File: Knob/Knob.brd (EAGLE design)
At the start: 36.3 x 29.8 mm, 18 parts, among them SW1 TopUp EC12PLRGBSDVBF-D, U1 ATTINY48/88-TQFP

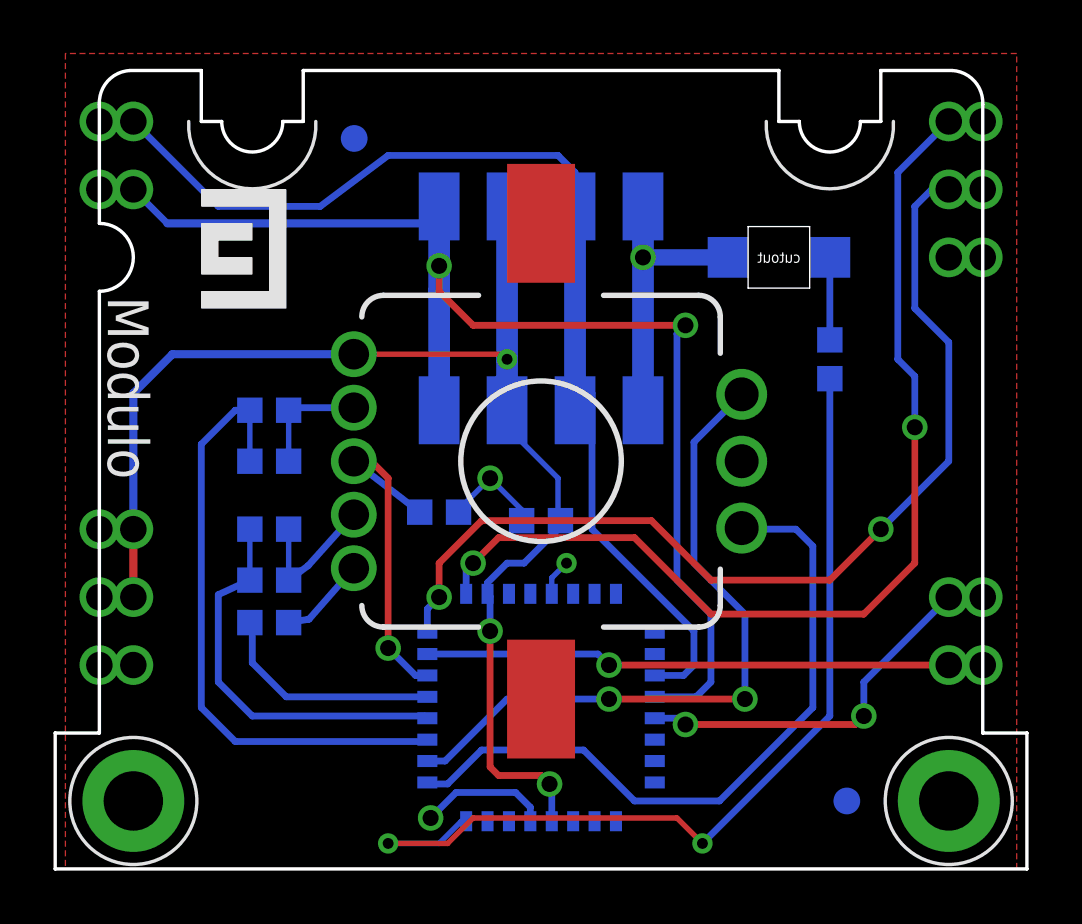
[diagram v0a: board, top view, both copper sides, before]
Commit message: Check point of current PCB designs. Among other things I think this change includes rewiring of programming lines on many of the boards,.
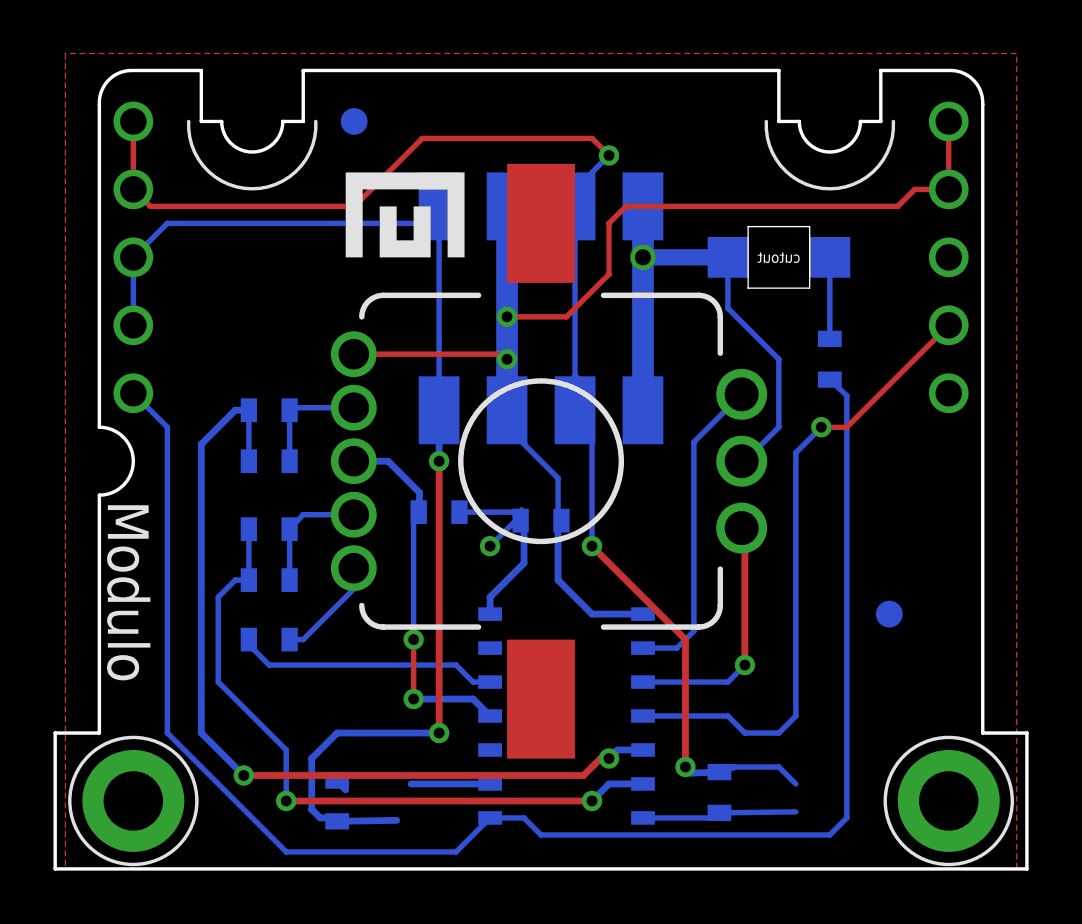
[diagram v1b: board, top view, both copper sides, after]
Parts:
- removed U$1: (no value), Modulo:LOGO-SMALL
- removed U1: ATTINY48/88-TQFP, Modulo:TQFP-32
- added R8, R9: 150Ω, Modulo:0603
- added U2: ATTINY841, Modulo:SOIC-14
- moved F1 7.16 mm to (30.8, 9.53)
- moved U$3 6.67 mm to (12.4, 23.5), turned to 0 degrees
- moved U$2 2.84 mm to (6.99, 21.0), flipped to the bottom, turned to 0 degrees
- moved F2 0.64 mm to (10.8, 27.9)
- moved R2 0.63 mm to (7.62, 8.57)
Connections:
- removed net LED: R7.2, U1.8
- removed net MISO: PCB1.MISO, U1.16
- removed net MOSI: PCB1.MOSI, U1.15
- removed net SCK: PCB1.CLK, U1.17
- new net MISO/LED: PCB1.MISO, R7.2, U2.8
- new net SCL/SCK: R8.2, U2.9
- new net SDA/MOSI: R9.2, U2.7
- net A: now also U2.3; no longer U1.9
- net B: now also U2.2; no longer U1.10
- net BLUE: now also U2.5; no longer U1.11
- net GND: now also U2.14; no longer U1.21, U1.5
- net GREEN: now also U2.6; no longer U1.12
- net RED: now also U2.12; no longer U1.13
- net RESET: now also U2.4; no longer U1.29
- net SCL: now also PCB1.CLK, R8.1; no longer U1.28
- net SDA: now also PCB1.MOSI, R9.1; no longer U1.27
- net SW: now also U2.11; no longer U1.14
- net VCC: now also U2.1; no longer U1.18, U1.4
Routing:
- net MISO/LED: track 0.00 -> 58.2 mm
- net SCK: track 37.7 -> 0.00 mm, vias 2 -> 0
- net MISO: track 36.8 -> 0.00 mm, vias 2 -> 0
- net LED: track 35.1 -> 0.00 mm, vias 2 -> 0
- net MOSI: track 19.7 -> 0.00 mm, vias 1 -> 0
- net A: track 26.2 -> 9.30 mm, vias 0 -> 1
- net B: track 25.7 -> 11.8 mm, vias 2 -> 0
- net SDA: track 43.1 -> 54.7 mm, vias 0 -> 3
- net GREEN: track 14.8 -> 25.6 mm, vias 0 -> 2
- net RESET: track 13.8 -> 23.8 mm, vias 2 -> 1
- net BLUE: track 23.5 -> 32.7 mm, vias 0 -> 2
- net GND: track 20.9 -> 28.5 mm, vias 4 -> 2
- net SDA/MOSI: track 0.00 -> 5.78 mm
- net SCL/SCK: track 0.00 -> 3.42 mm
- net SCL: track 47.8 -> 44.6 mm
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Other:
- outline, holes or cut-outs redrawn

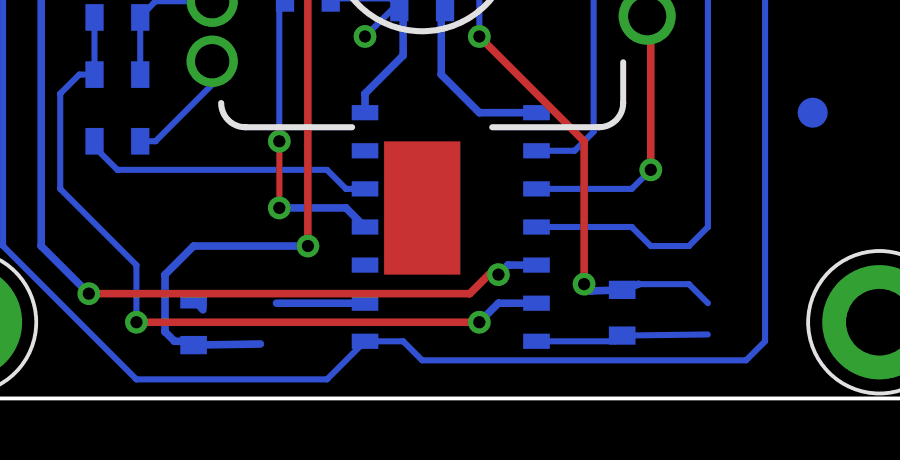
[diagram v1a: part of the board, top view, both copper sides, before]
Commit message: Fixed missing trace on SCL/SCK net.
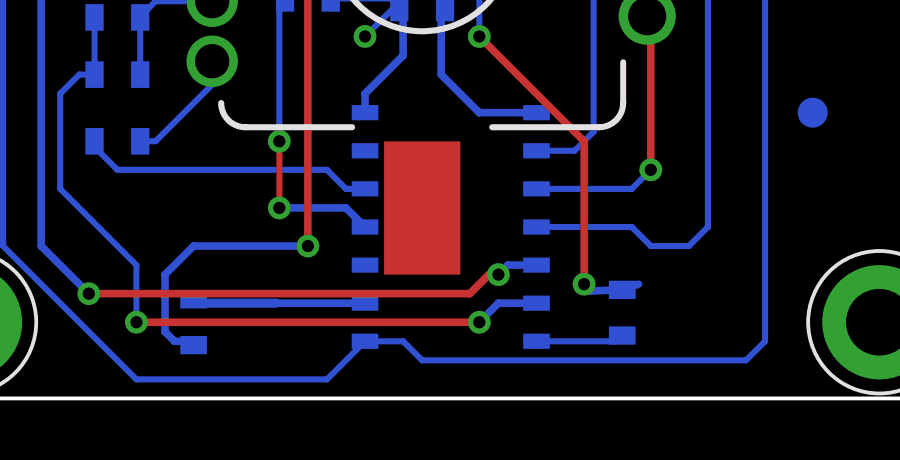
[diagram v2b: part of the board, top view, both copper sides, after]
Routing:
- net SDA/MOSI: track 5.78 -> 2.93 mm
- net SDA: track 54.7 -> 52.1 mm
- net SCL/SCK: track 3.42 -> 5.84 mm
- net SCL: track 44.6 -> 42.4 mm
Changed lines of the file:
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@@
 <layer number="17" name="Pads" color="2" fill="1" visible="yes" active="yes"/>
 <layer number="18" name="Vias" color="2" fill="1" visible="yes" active="yes"/>
-<layer number="19" name="Unrouted" color="6" fill="1" visible="no" active="yes"/>
+<layer number="19" name="Unrouted" color="6" fill="1" visible="yes" active="yes"/>
 <layer number="20" name="Dimension" color="15" fill="1" visible="yes" active="yes"/>
 <layer number="21" name="tPlace" color="7" fill="1" visible="yes" active="yes"/>
@@
 <contactref element="JP1" pad="P$7"/>
 <contactref element="R8" pad="1"/>
-<wire x1="10.16" y1="1.778" x2="12.3869" y2="1.815" width="0.254" layer="16"/>
 <via x="13.97" y="5.08" extent="1-16" drill="0.4064"/>
 <wire x1="13.97" y1="5.08" x2="13.97" y2="15.24" width="0.254" layer="1"/>
@@
 <wire x1="19.05" y1="18.415" x2="19.05" y2="17.145" width="0.2032" layer="16"/>
 <contactref element="R9" pad="1"/>
-<wire x1="27.305" y1="3.175" x2="26.67" y2="3.81" width="0.2032" layer="16"/>
-<wire x1="26.67" y1="3.81" x2="24.9925" y2="3.81" width="0.2032" layer="16"/>
 <wire x1="24.9925" y1="3.81" x2="24.4475" y2="3.6195" width="0.254" layer="16"/>
 <wire x1="24.4475" y1="3.6195" x2="23.405" y2="3.5825" width="0.254" layer="16"/>
@@
 <contactref element="R9" pad="2"/>
 <contactref element="U2" pad="7"/>
-<wire x1="24.4475" y1="2.0955" x2="27.3006" y2="2.1325" width="0.2032" layer="16"/>
 <wire x1="21.59" y1="1.905" x2="24.22" y2="1.905" width="0.2032" layer="16"/>
 <wire x1="24.22" y1="1.905" x2="24.4475" y2="2.0955" width="0.2032" layer="16"/>
@@
 <contactref element="U2" pad="9"/>
 <wire x1="15.875" y1="3.175" x2="12.9231" y2="3.175" width="0.254" layer="16"/>
-<wire x1="10.4731" y1="2.9519" x2="10.16" y2="3.302" width="0.254" layer="16"/>
-<wire x1="10.4731" y1="2.9519" x2="12.9231" y2="3.175" width="0" layer="19" extent="16-16"/>
+<wire x1="12.9231" y1="3.175" x2="10.16" y2="3.175" width="0.3048" layer="16"/>
+<wire x1="10.16" y1="3.175" x2="10.16" y2="3.302" width="0.3048" layer="16"/>
 </signal>
 <signal name="MISO/LED">

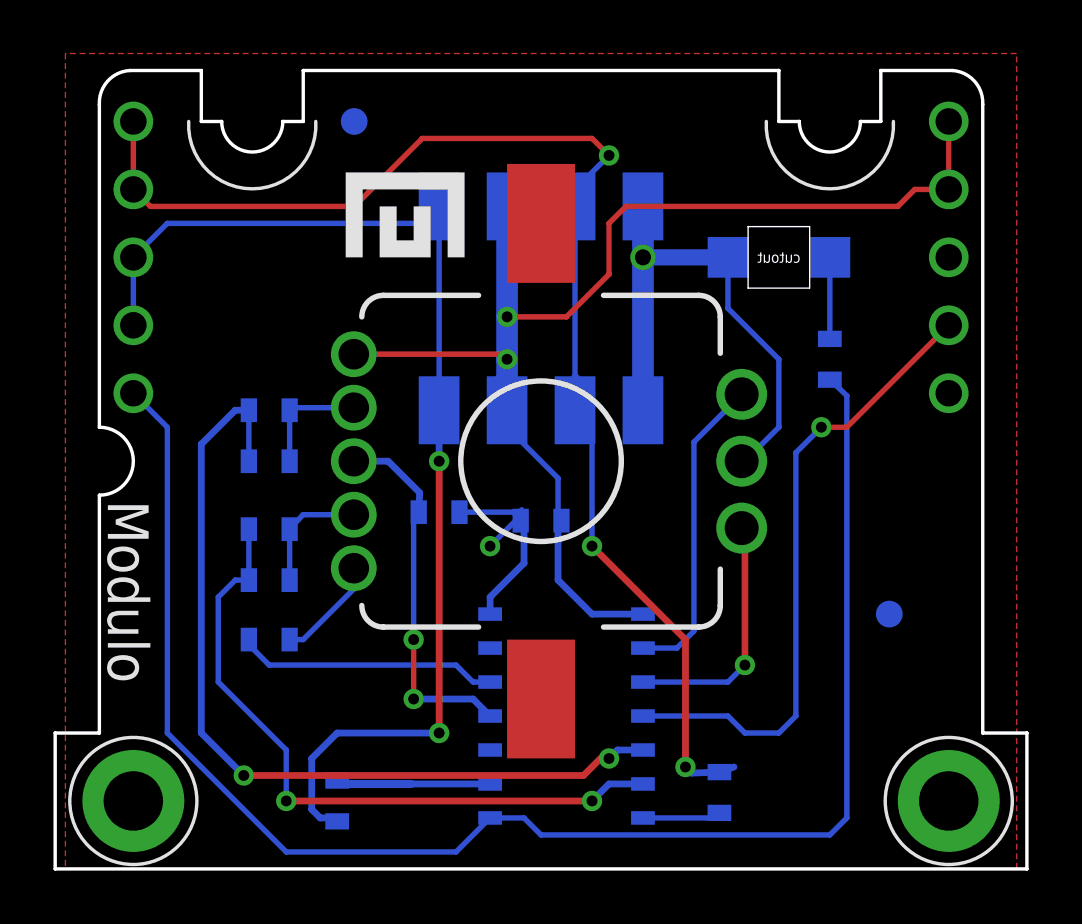
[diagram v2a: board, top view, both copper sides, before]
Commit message: Added parallel resistor on red channel for better white balance. Moved status LED to opposite side of the board next to logo Updated to new 0603 footprint.
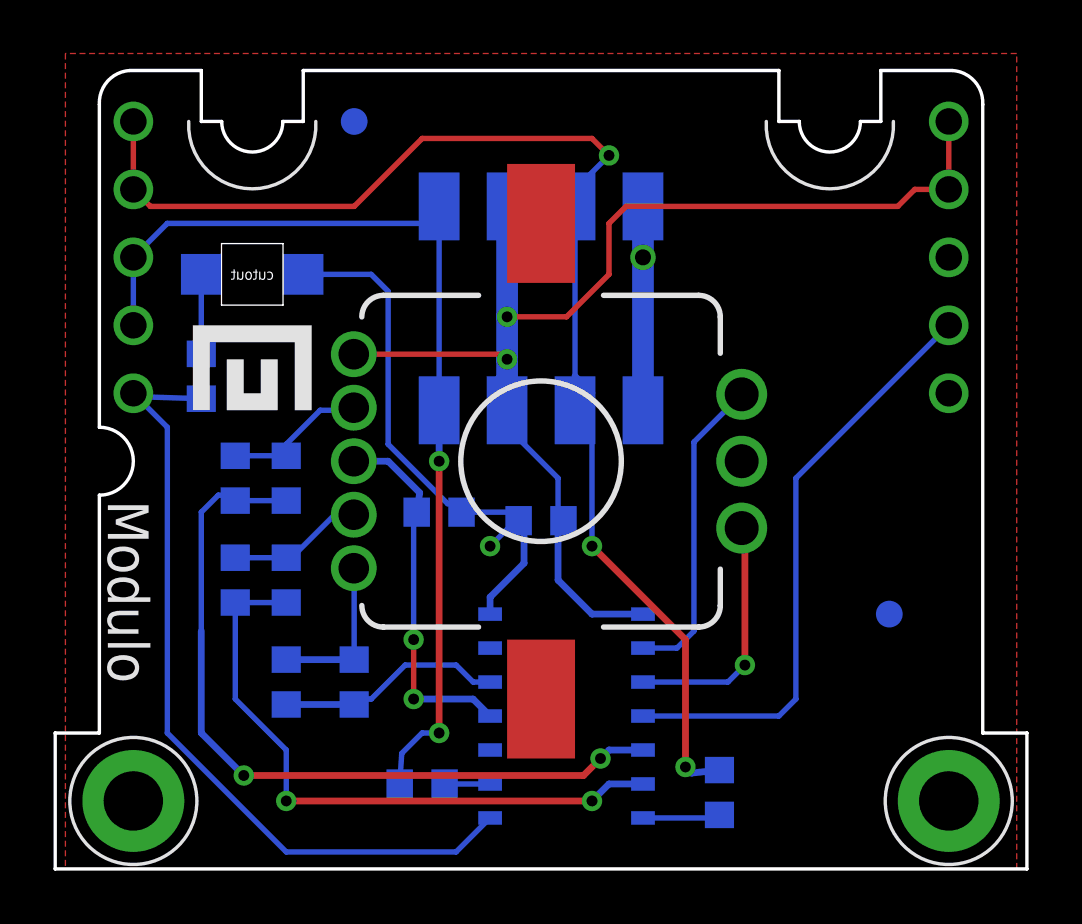
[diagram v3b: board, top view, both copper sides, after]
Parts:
- added R10: 150Ω, Modulo:0603
- moved R7 23.5 mm to (5.08, 18.4)
- moved U$2 21.6 mm to (28.6, 21.6)
- moved LED1 19.7 mm to (6.99, 22.2), turned to 180 degrees
- moved U$3 8.08 mm to (6.67, 17.8)
- moved R8 3.24 mm to (13.3, 3.17), turned to 180 degrees
- moved R6 2.84 mm to (6.35, 14.6), turned to 270 degrees
- moved R4 2.01 mm to (8.26, 10.8), turned to 270 degrees
- moved R2 1.71 mm to (8.26, 6.99), turned to 270 degrees
- moved R3 1.27 mm to (6.35, 10.8), turned to 270 degrees
- moved R5 0.90 mm to (8.26, 14.6), turned to 270 degrees
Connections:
- net N$4: now also R10.1
- net RED: now also R10.2
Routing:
- net MISO/LED: track 58.2 -> 30.3 mm
- net SCL: track 42.4 -> 37.0 mm
- net SCL/SCK: track 5.84 -> 1.70 mm
- net BLUE: track 32.7 -> 29.4 mm
- net N$4: track 3.97 -> 5.96 mm
- net GREEN: track 25.6 -> 23.7 mm
- net RESET: track 23.8 -> 22.3 mm, vias 1 -> 0
- net RED: track 9.80 -> 8.52 mm
- net N$6: track 4.36 -> 5.43 mm
- net GND: track 28.5 -> 29.4 mm
- net N$5: track 4.54 -> 5.23 mm
- net SDA: track 52.1 -> 51.5 mm

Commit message: Increased trace width to 10mil from 8 Bumped version number to 6
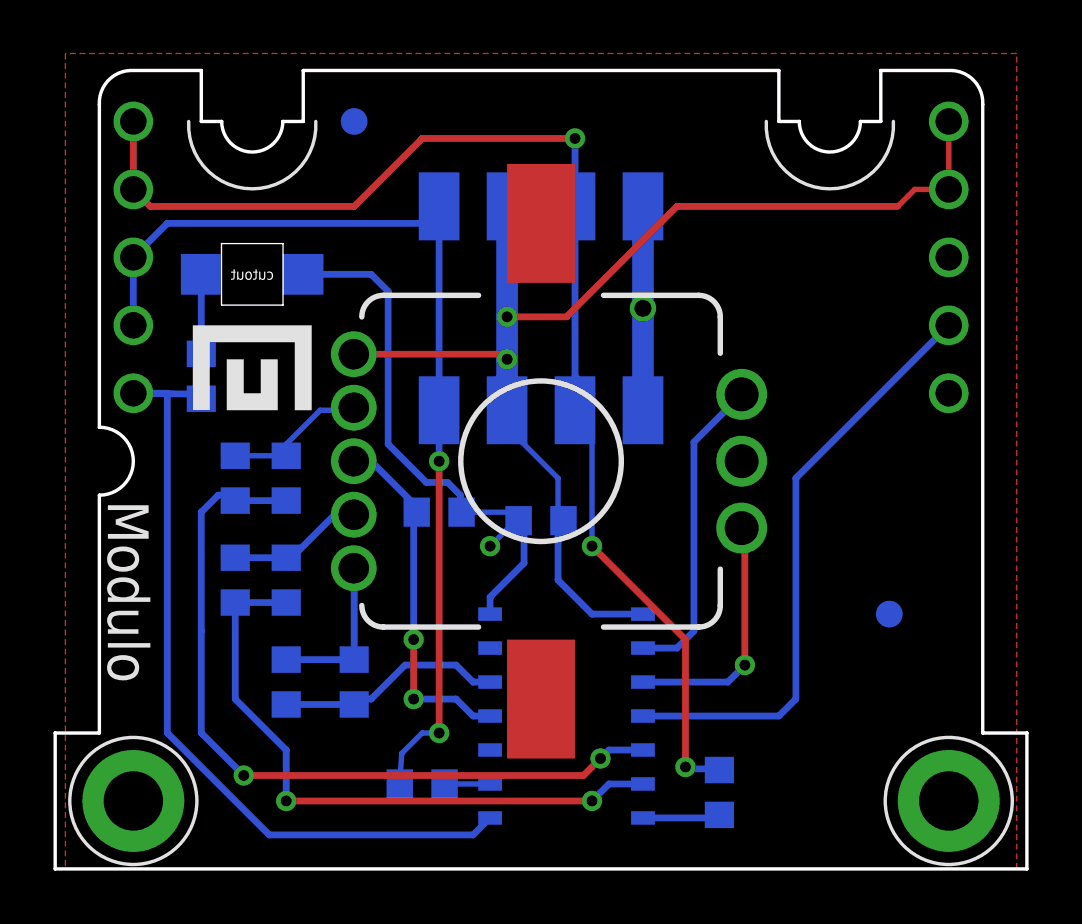
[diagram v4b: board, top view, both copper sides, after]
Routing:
- net SDA: track 51.5 -> 50.1 mm
- net VCC: track 48.4 -> 47.3 mm

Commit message: Various changes
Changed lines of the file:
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@@
 </class>
 </classes>
-<designrules name="LaenPCBOrder">
+<designrules name="Modulo">
 <description language="de">&lt;b&gt;EAGLE Design Rules&lt;/b&gt;
 &lt;p&gt;
@@
 Einstellungen hier und speichern die Design Rules unter
 einem neuen Namen ab.</description>
-<description language="en">&lt;b&gt;Laen's PCB Order Design Rules&lt;/b&gt;
-&lt;p&gt;
-Please make sure your boards conform to these design rules.</description>
+<description language="en">&lt;b&gt;Modulo Design Rules&lt;/b&gt;
+</description>
 <param name="layerSetup" value="(1*16)"/>
 <param name="mtCopper" value="0.0356mm 0.0356mm 0.0356mm 0.0356mm 0.0356mm 0.0356mm 0.0356mm 0.0356mm 0.0356mm 0.0356mm 0.0356mm 0.0356mm 0.0356mm 0.0356mm 0.0356mm 0.0356mm"/>
@@
 <param name="mlMinCreamFrame" value="0mil"/>
 <param name="mlMaxCreamFrame" value="0mil"/>
-<param name="mlViaStopLimit" value="0mil"/>
+<param name="mlViaStopLimit" value="25mil"/>
 <param name="srRoundness" value="0"/>
 <param name="srMinRoundness" value="0mil"/>
@@
 <wire x1="17.055" y1="13.245" x2="15.875" y2="12.065" width="0.2032" layer="16"/>
 <via x="15.875" y="12.065" extent="1-16" drill="0.4064"/>
-<wire x1="8.885" y1="22.225" x2="11.43" y2="22.225" width="0.254" layer="16"/>
+<wire x1="8.763" y1="22.225" x2="11.43" y2="22.225" width="0.254" layer="16"/>
 <wire x1="11.43" y1="22.225" x2="12.065" y2="21.59" width="0.254" layer="16"/>
 <wire x1="12.065" y1="21.59" x2="12.065" y2="15.875" width="0.254" layer="16"/>
@@
 <contactref element="R7" pad="1"/>
 <contactref element="LED1" pad="A"/>
-<wire x1="5.08" y1="19.2532" x2="5.08" y2="22.225" width="0.254" layer="16"/>
+<wire x1="5.08" y1="19.2532" x2="5.207" y2="22.225" width="0.254" layer="16"/>
 </signal>
 <signal name="VCC">

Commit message: Various small tweaks based on testing and feedback from manufacturer.
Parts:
- R8, R9: value 150Ω -> 0Ω
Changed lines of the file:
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@@
 <attribute name="VALUE" x="18.7325" y="10.795" size="0.635" layer="28" rot="MR0"/>
 </element>
-<element name="R8" library="Modulo" package="0603" value="150Ω" x="13.335" y="3.175" smashed="yes" rot="MR180">
-<attribute name="PARTNUM" value="ERJ-3EKF1500V" x="13.335" y="3.175" size="1.778" layer="28" rot="MR180" display="off"/>
+<element name="R8" library="Modulo" package="0603" value="0Ω" x="13.335" y="3.175" smashed="yes" rot="MR180">
+<attribute name="PARTNUM" value="ERJ-3GEY0R00V" x="13.335" y="3.175" size="1.778" layer="28" rot="MR180" display="off"/>
 <attribute name="NAME" x="11.8745" y="3.048" size="0.635" layer="26" font="vector" rot="MR0"/>
-<attribute name="VALUE" x="14.6685" y="1.778" size="0.635" layer="28" font="vector" rot="MR0"/>
+<attribute name="VALUE" value="0Ω" x="14.6685" y="1.778" size="0.635" layer="28" font="vector" rot="MR0"/>
 </element>
-<element name="R9" library="Modulo" package="0603" value="150Ω" x="24.4475" y="2.8575" smashed="yes" rot="MR270">
-<attribute name="PARTNUM" value="ERJ-3EKF1500V" x="24.4475" y="2.8575" size="1.778" layer="28" rot="MR270" display="off"/>
+<element name="R9" library="Modulo" package="0603" value="0Ω" x="24.4475" y="2.8575" smashed="yes" rot="MR270">
+<attribute name="PARTNUM" value="ERJ-3GEY0R00V" x="24.4475" y="2.8575" size="1.778" layer="28" rot="MR270" display="off"/>
 <attribute name="NAME" x="23.6855" y="5.04825" size="0.635" layer="26" font="vector" rot="MR180"/>
-<attribute name="VALUE" x="23.4315" y="1.397" size="0.635" layer="28" font="vector" rot="MR180"/>
+<attribute name="VALUE" value="0Ω" x="23.4315" y="1.397" size="0.635" layer="28" font="vector" rot="MR180"/>
 </element>
 <element name="R10" library="Modulo" package="0603" value="150Ω" x="10.795" y="6.985" smashed="yes" rot="MR270">

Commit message: Added unique board prefixes to part numbers due to CM requirements
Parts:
- renumbered C1 to 6-C1, F1 to 6-F1, F2 to 6-F2, JP1 to 6-JP1, LED1 to 6-LED1, PCB1 to 6-PCB1, R1 to 6-R1, R10 to 6-R10, R2 to 6-R2, R3 to 6-R3, R4 to 6-R4, R5 to 6-R5, R6 to 6-R6, R7 to 6-R7, R8 to 6-R8, R9 to 6-R9, SW1 to 6-SW1, U2 to 6-U2
